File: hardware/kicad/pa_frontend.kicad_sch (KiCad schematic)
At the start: 0 parts

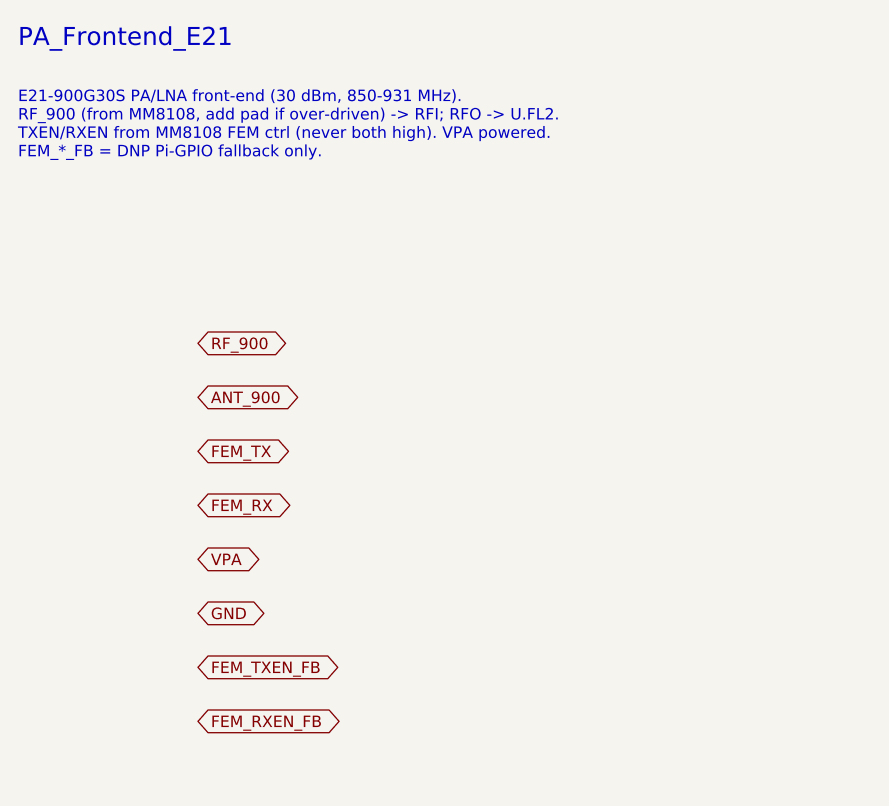
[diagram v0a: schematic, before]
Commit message: Deepen design to component level + fix EEPROM power rail
- Fix: HAT ID EEPROM (U6) now powered from Pi header 3V3 (3V3_PI, pin 1)
  so it is readable at boot before the HAT's own 3V3 comes up (was
  incorrectly on the HAT 3V3 regulator).
- Add docs/SCHEMATIC.md: component-level subcircuits for every block
  (refdes + values + nets) — buck-boost/3V3 FB dividers, MM8108 SPI
  termination/pulls, E21 RF DC-blocks/attenuator pad/T-R pulldowns,
  NEO-M9N active-antenna bias via VCC_RF, ID EEPROM (WP default).
- Add docs/BRINGUP.md: stage-gated power-on + RF test plan (don't key
  the 1W PA until rails/drive-level/FEM-timing verified).
- Add GNSS VCC_RF antenna bias + +3V3_GNSS ferrite to the net list.
- Enrich KiCad sub-sheets with per-block refdes notes and the new nets;
  regenerate scaffold (KiCad 10 format, S-expression balance re-checked).
- BOM: concrete passives (RF DC-blocks, attenuator pad, ferrite, TVS,
  FB dividers, WP jumper).

https://claude.ai/code/session_015nkkW85U3sPf5mcvrsMw7T
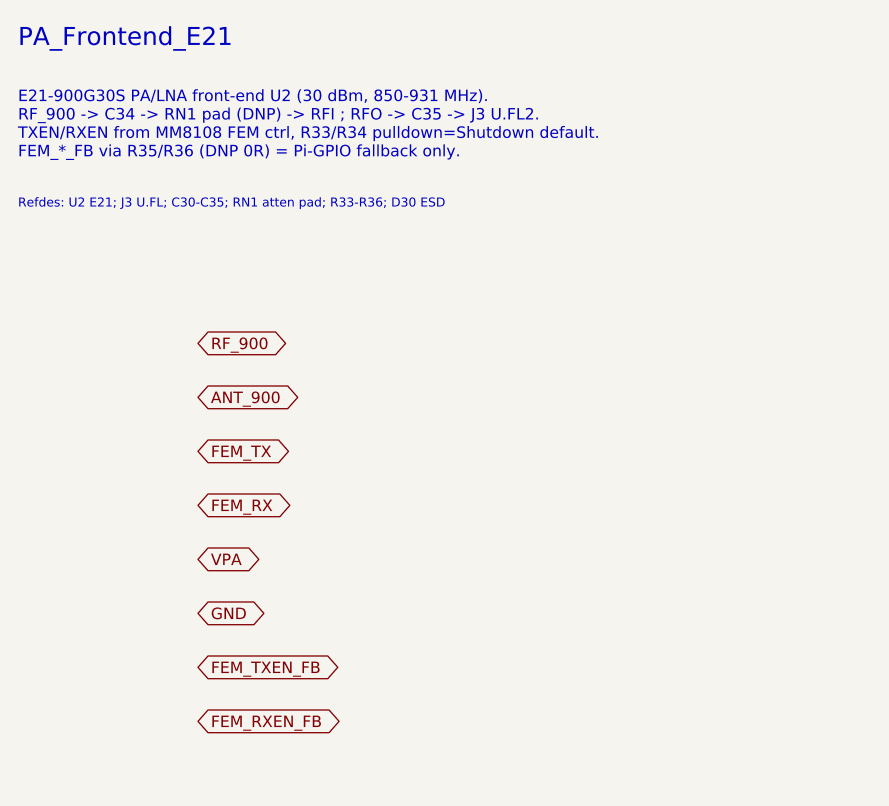
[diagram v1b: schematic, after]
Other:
- note added: "E21-900G30S PA/LNA front-end U2 (30 dBm, 850-931 MHz). RF_900 -> C34 -> RN1 pad (DNP) -> RFI ; RFO -> C35 -> J3 U.FL2. TXEN/RXEN from MM8108 FEM ctrl, R33/R34 pulldown=Shutdown default. FEM_*_FB via R35/R36 (DNP 0R) = Pi-GPIO fallback only."
- note added: "Refdes: U2 E21; J3 U.FL; C30-C35; RN1 atten pad; R33-R36; D30 ESD"
- note removed: "E21-900G30S PA/LNA front-end (30 dBm, 850-931 MHz). RF_900 (from MM8108, add pad if over-driven) -> RFI; RFO -> U.FL2. TXEN/RXEN from MM8108 FEM ctrl (never both high). VPA powered. FEM_*_FB = DNP Pi-GPIO fallback only."
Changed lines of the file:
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@@
 	(paper "A4")
 	(text "PA_Frontend_E21" (exclude_from_sim no) (at 20 15 0) (effects (font (size 2 2) (thickness 0.3)) (justify left top)))
-	(text "E21-900G30S PA/LNA front-end (30 dBm, 850-931 MHz).\nRF_900 (from MM8108, add pad if over-driven) -> RFI; RFO -> U.FL2.\nTXEN/RXEN from MM8108 FEM ctrl (never both high). VPA powered.\nFEM_*_FB = DNP Pi-GPIO fallback only." (exclude_from_sim no) (at 20 22 0) (effects (font (size 1.27 1.27)) (justify left top)))
+	(text "E21-900G30S PA/LNA front-end U2 (30 dBm, 850-931 MHz).\nRF_900 -> C34 -> RN1 pad (DNP) -> RFI ; RFO -> C35 -> J3 U.FL2.\nTXEN/RXEN from MM8108 FEM ctrl, R33/R34 pulldown=Shutdown default.\nFEM_*_FB via R35/R36 (DNP 0R) = Pi-GPIO fallback only." (exclude_from_sim no) (at 20 22 0) (effects (font (size 1.27 1.27)) (justify left top)))
+	(text "Refdes: U2 E21; J3 U.FL; C30-C35; RN1 atten pad; R33-R36; D30 ESD" (exclude_from_sim no) (at 20 34 0) (effects (font (size 1.0 1.0)) (justify left top)))
 	(global_label "RF_900" (shape bidirectional) (at 40 50 0) (fields_autoplaced yes) (effects (font (size 1.27 1.27)) (justify left)))
 	(global_label "ANT_900" (shape bidirectional) (at 40 56 0) (fields_autoplaced yes) (effects (font (size 1.27 1.27)) (justify left)))

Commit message: Add gap-analysis components (datasheet-grounded) + RTC
Read the uploaded datasheets (MM8108-MF15457, E21-900G30S, NEO-M9N-00B)
and resolved the component gaps:

- #1/#2 RESOLVED by the module: MF15457 is self-contained (internal
  clock+PMU+PA); only needs VBAT/VBAT_TX/VDDIO 3.0-3.6 V. No external SoC
  inductors, 1V8/1V2 rails, or TCXO.
- VPA fixed at 5.0 V (E21 needs 4.75-5.25 V, ~620 mA TX, +20 dBm in ->
  +30 dBm out, 12 dB gain). Real pinouts wired (module 38-pin; E21
  pin6=PIN xcvr, pin9=ANT).
- Architecture finding: module has integrated PA + single ANT pin and NO
  hardware T/R FEM line. External E21 now needs (a) ~3-5 dB drive pad,
  (b) T/R control via module GPIO0/1 toggled by OpenMANET FW (or RF-sense
  auto-T/R fallback), and (c) end-product recertification at +30 dBm.

Added components:
- N3 900 MHz harmonic LPF (FL2); N4 inrush soft-start load switch (U10);
  N5 supervisor (U11); N6 radio-rail load switch (U12, OpenMANET
  power-gpios); N7 RF shields; N8 GNSS antenna ESD (D8); N9 status LEDs;
  N10 E21 thermal relief.
- RTC: RV-3028-C7 (U13) on I2C1 0x52 with a soldered rechargeable cell
  (BT1, trickle-charged) per request; added to the device-tree overlay.
- Declined per request: debug UART/JTAG pads, test points.

Updated docs (new COMPONENTS_GAP.md; DECISIONS B1-B9; SCHEMATIC; BOM;
POWER budget), netlist, overlay, and regenerated the KiCad 10 scaffold
with the new nets. Committed the vendor datasheets under hardware/.

https://claude.ai/code/session_015nkkW85U3sPf5mcvrsMw7T
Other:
- note added: "E21-900G30S U2 (VCC=5.0V, ~620mA TX, +20dBm in->+30dBm out). RF_900 (module ANT +22..25dBm) -> C34 -> RN1 ~3-5dB pad -> PIN(6). ANT(9) -> FL2 LPF -> C35 -> J3 U.FL2 (+30dBm harmonic compliance). TX_EN(3)/RX_EN(4) <- PA_TX/RX_CTL; R33/R34 pulldown=Shutdown default."
- note added: "Refdes: U2 E21; J3 U.FL; FL2 LPF; RN1 pad; C30-C35; R33-R36; D30 ESD"
- note removed: "E21-900G30S PA/LNA front-end U2 (30 dBm, 850-931 MHz). RF_900 -> C34 -> RN1 pad (DNP) -> RFI ; RFO -> C35 -> J3 U.FL2. TXEN/RXEN from MM8108 FEM ctrl, R33/R34 pulldown=Shutdown default. FEM_*_FB via R35/R36 (DNP 0R) = Pi-GPIO fallback only."
- note removed: "Refdes: U2 E21; J3 U.FL; C30-C35; RN1 atten pad; R33-R36; D30 ESD"
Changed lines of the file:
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@@
 	(paper "A4")
 	(text "PA_Frontend_E21" (exclude_from_sim no) (at 20 15 0) (effects (font (size 2 2) (thickness 0.3)) (justify left top)))
-	(text "E21-900G30S PA/LNA front-end U2 (30 dBm, 850-931 MHz).\nRF_900 -> C34 -> RN1 pad (DNP) -> RFI ; RFO -> C35 -> J3 U.FL2.\nTXEN/RXEN from MM8108 FEM ctrl, R33/R34 pulldown=Shutdown default.\nFEM_*_FB via R35/R36 (DNP 0R) = Pi-GPIO fallback only." (exclude_from_sim no) (at 20 22 0) (effects (font (size 1.27 1.27)) (justify left top)))
-	(text "Refdes: U2 E21; J3 U.FL; C30-C35; RN1 atten pad; R33-R36; D30 ESD" (exclude_from_sim no) (at 20 34 0) (effects (font (size 1.0 1.0)) (justify left top)))
+	(text "E21-900G30S U2 (VCC=5.0V, ~620mA TX, +20dBm in->+30dBm out).\nRF_900 (module ANT +22..25dBm) -> C34 -> RN1 ~3-5dB pad -> PIN(6).\nANT(9) -> FL2 LPF -> C35 -> J3 U.FL2 (+30dBm harmonic compliance).\nTX_EN(3)/RX_EN(4) <- PA_TX/RX_CTL; R33/R34 pulldown=Shutdown default." (exclude_from_sim no) (at 20 22 0) (effects (font (size 1.27 1.27)) (justify left top)))
+	(text "Refdes: U2 E21; J3 U.FL; FL2 LPF; RN1 pad; C30-C35; R33-R36; D30 ESD" (exclude_from_sim no) (at 20 34 0) (effects (font (size 1.0 1.0)) (justify left top)))
 	(global_label "RF_900" (shape bidirectional) (at 40 50 0) (fields_autoplaced yes) (effects (font (size 1.27 1.27)) (justify left)))
 	(global_label "ANT_900" (shape bidirectional) (at 40 56 0) (fields_autoplaced yes) (effects (font (size 1.27 1.27)) (justify left)))
-	(global_label "FEM_TX" (shape bidirectional) (at 40 62 0) (fields_autoplaced yes) (effects (font (size 1.27 1.27)) (justify left)))
-	(global_label "FEM_RX" (shape bidirectional) (at 40 68 0) (fields_autoplaced yes) (effects (font (size 1.27 1.27)) (justify left)))
+	(global_label "PA_TX_CTL" (shape bidirectional) (at 40 62 0) (fields_autoplaced yes) (effects (font (size 1.27 1.27)) (justify left)))
+	(global_label "PA_RX_CTL" (shape bidirectional) (at 40 68 0) (fields_autoplaced yes) (effects (font (size 1.27 1.27)) (justify left)))
 	(global_label "VPA" (shape bidirectional) (at 40 74 0) (fields_autoplaced yes) (effects (font (size 1.27 1.27)) (justify left)))
 	(global_label "GND" (shape bidirectional) (at 40 80 0) (fields_autoplaced yes) (effects (font (size 1.27 1.27)) (justify left)))

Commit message: Make E21 PA a DNP/optional Variant B; default to module-only
Deployment is ground/handheld/vehicle (NLOS), where the E21's +3 dB buys
only ~20% range (LINK_BUDGET) against ~620 mA + heat + recert + RX-rate
risk. So restructure as one PCB with two BOM builds:

- Variant A (DEFAULT): module-only ~27 dBm via OpenMANET BCF. E21,
  buck-boost (VPA), LPF and drive pad are DNP; an RF bypass (C_BYP)
  carries the module ANT straight to U.FL #2. Low power (~0.35 A), good
  for battery handhelds, stays on the module's modular cert.
- Variant B (OPTIONAL): populate E21 + VPA + LPF + T/R for +30 dBm
  extended range (fixed/elevated LoS); remove C_BYP; needs custom-BCF
  FEM GPIO control + end-product recert. No respin required.

Updated DECISIONS (B5/B10 resolved + new §C variants & order), SCHEMATIC,
POWER (default-build budget), BOM (variant tags + C_BYP), netlist, README,
and regenerated the KiCad scaffold (bypass net + silk tags).

https://claude.ai/code/session_015nkkW85U3sPf5mcvrsMw7T
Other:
- note added: "E21-900G30S U2 -- VARIANT B (DNP DEFAULT). +30dBm extended-range opt. Variant A (default): module ANT -> C_BYP RF bypass -> J3 U.FL2 (no PA). Variant B: RF_900 -> C34 -> RN1 ~3-5dB pad -> PIN(6); ANT(9)->FL2->U.FL2. TX_EN(3)/RX_EN(4) <- PA_TX/RX_CTL (BCF); R33/R34 pulldown=off default."
- note added: "Refdes: U2 E21; C_BYP bypass(VarA); J3 U.FL; FL2 LPF; RN1 pad; C30-C35; R33-R36; D30 ESD"
- note removed: "E21-900G30S U2 (VCC=5.0V, ~620mA TX, +20dBm in->+30dBm out). RF_900 (module ANT +22..25dBm) -> C34 -> RN1 ~3-5dB pad -> PIN(6). ANT(9) -> FL2 LPF -> C35 -> J3 U.FL2 (+30dBm harmonic compliance). TX_EN(3)/RX_EN(4) <- PA_TX/RX_CTL; R33/R34 pulldown=Shutdown default."
- note removed: "Refdes: U2 E21; J3 U.FL; FL2 LPF; RN1 pad; C30-C35; R33-R36; D30 ESD"
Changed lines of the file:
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@@
 	(paper "A4")
 	(text "PA_Frontend_E21" (exclude_from_sim no) (at 20 15 0) (effects (font (size 2 2) (thickness 0.3)) (justify left top)))
-	(text "E21-900G30S U2 (VCC=5.0V, ~620mA TX, +20dBm in->+30dBm out).\nRF_900 (module ANT +22..25dBm) -> C34 -> RN1 ~3-5dB pad -> PIN(6).\nANT(9) -> FL2 LPF -> C35 -> J3 U.FL2 (+30dBm harmonic compliance).\nTX_EN(3)/RX_EN(4) <- PA_TX/RX_CTL; R33/R34 pulldown=Shutdown default." (exclude_from_sim no) (at 20 22 0) (effects (font (size 1.27 1.27)) (justify left top)))
-	(text "Refdes: U2 E21; J3 U.FL; FL2 LPF; RN1 pad; C30-C35; R33-R36; D30 ESD" (exclude_from_sim no) (at 20 34 0) (effects (font (size 1.0 1.0)) (justify left top)))
+	(text "E21-900G30S U2 -- VARIANT B (DNP DEFAULT). +30dBm extended-range opt.\nVariant A (default): module ANT -> C_BYP RF bypass -> J3 U.FL2 (no PA).\nVariant B: RF_900 -> C34 -> RN1 ~3-5dB pad -> PIN(6); ANT(9)->FL2->U.FL2.\nTX_EN(3)/RX_EN(4) <- PA_TX/RX_CTL (BCF); R33/R34 pulldown=off default." (exclude_from_sim no) (at 20 22 0) (effects (font (size 1.27 1.27)) (justify left top)))
+	(text "Refdes: U2 E21; C_BYP bypass(VarA); J3 U.FL; FL2 LPF; RN1 pad; C30-C35; R33-R36; D30 ESD" (exclude_from_sim no) (at 20 34 0) (effects (font (size 1.0 1.0)) (justify left top)))
 	(global_label "RF_900" (shape bidirectional) (at 40 50 0) (fields_autoplaced yes) (effects (font (size 1.27 1.27)) (justify left)))
 	(global_label "ANT_900" (shape bidirectional) (at 40 56 0) (fields_autoplaced yes) (effects (font (size 1.27 1.27)) (justify left)))
-	(global_label "PA_TX_CTL" (shape bidirectional) (at 40 62 0) (fields_autoplaced yes) (effects (font (size 1.27 1.27)) (justify left)))
-	(global_label "PA_RX_CTL" (shape bidirectional) (at 40 68 0) (fields_autoplaced yes) (effects (font (size 1.27 1.27)) (justify left)))
-	(global_label "VPA" (shape bidirectional) (at 40 74 0) (fields_autoplaced yes) (effects (font (size 1.27 1.27)) (justify left)))
-	(global_label "GND" (shape bidirectional) (at 40 80 0) (fields_autoplaced yes) (effects (font (size 1.27 1.27)) (justify left)))
-	(global_label "FEM_TXEN_FB" (shape bidirectional) (at 40 86 0) (fields_autoplaced yes) (effects (font (size 1.27 1.27)) (justify left)))
-	(global_label "FEM_RXEN_FB" (shape bidirectional) (at 40 92 0) (fields_autoplaced yes) (effects (font (size 1.27 1.27)) (justify left)))
+	(global_label "C_BYP" (shape bidirectional) (at 40 62 0) (fields_autoplaced yes) (effects (font (size 1.27 1.27)) (justify left)))
+	(global_label "PA_TX_CTL" (shape bidirectional) (at 40 68 0) (fields_autoplaced yes) (effects (font (size 1.27 1.27)) (justify left)))
+	(global_label "PA_RX_CTL" (shape bidirectional) (at 40 74 0) (fields_autoplaced yes) (effects (font (size 1.27 1.27)) (justify left)))
+	(global_label "VPA" (shape bidirectional) (at 40 80 0) (fields_autoplaced yes) (effects (font (size 1.27 1.27)) (justify left)))
+	(global_label "GND" (shape bidirectional) (at 40 86 0) (fields_autoplaced yes) (effects (font (size 1.27 1.27)) (justify left)))
+	(global_label "FEM_TXEN_FB" (shape bidirectional) (at 40 92 0) (fields_autoplaced yes) (effects (font (size 1.27 1.27)) (justify left)))
+	(global_label "FEM_RXEN_FB" (shape bidirectional) (at 40 98 0) (fields_autoplaced yes) (effects (font (size 1.27 1.27)) (justify left)))
 )

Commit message: Pivot to MM8108-M20 primary / MF15457 fallback; retire external E21
Per the decision to make the MM8108-M20 the primary radio (with MF15457
as the build-today fallback) and retire the external E21 PA path:

Design:
- One radio site fed by the shared SPI/control nets accepts either module.
- Removed the E21 PA, 5V buck-boost (VPA), harmonic LPF, drive pad, T/R
  control, RF-sense VOX, and RF bypass. Both modules drive the antenna
  directly (M20 = integrated 28.5 dBm PA + 902-928 SAW, certified;
  MF15457 = ~27 dBm). Power collapses to a single 3V3 rail.
- Header GPIO4/6 (old FEM fallback) revert to spares; GPIO12/13 drive the
  status LEDs.
- M20 pinout/power/footprint held at placeholder pending its datasheet
  (B12); MF15457 pin-level detail stays the concrete baseline.

Docs updated: DECISIONS (A3 superseded, B11/B12 added, B2-B5/B10 retired,
new radio-options table + order), DESIGN, SCHEMATIC, POWER, RF, BOM,
INTERFACES, COMPONENTS_GAP, LINK_BUDGET, FIRMWARE_PA, BRINGUP, MECHANICAL,
README. Netlist, KiCad scaffold (sheets/silk/root note), and the OpenMANET
overlay/README updated to match. Scaffold regenerated and validated.

https://claude.ai/code/session_015nkkW85U3sPf5mcvrsMw7T
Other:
- note added: "900MHz RF OUTPUT / ANTENNA (E21 PA retired, B11). Radio ANT -> RF_900 -> C35 100pF DC-block -> ANT_900 -> J3 U.FL2. FL2 optional LPF = DNP (M20 has integ. SAW; MF15457 modular-certified). D30 low-C RF ESD clamp at the connector. Short 50ohm microstrip."
- note added: "RF_Out_Antenna"
- note added: "Refdes: J3 U.FL; C35 DC-block; FL2 LPF(DNP); D30 ESD"
- note removed: "E21-900G30S U2 -- VARIANT B (DNP DEFAULT). +30dBm extended-range opt. Variant A (default): module ANT -> C_BYP RF bypass -> J3 U.FL2 (no PA). Variant B: RF_900 -> C34 -> RN1 ~3-5dB pad -> PIN(6); ANT(9)->FL2->U.FL2. TX_EN(3)/RX_EN(4) <- PA_TX/RX_CTL (BCF); R33/R34 pulldown=off default."
- note removed: "PA_Frontend_E21"
- note removed: "Refdes: U2 E21; C_BYP bypass(VarA); J3 U.FL; FL2 LPF; RN1 pad; C30-C35; R33-R36; D30 ESD"
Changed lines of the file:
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@@
 	(generator_version "10.0")
 	(paper "A4")
-	(text "PA_Frontend_E21" (exclude_from_sim no) (at 20 15 0) (effects (font (size 2 2) (thickness 0.3)) (justify left top)))
-	(text "E21-900G30S U2 -- VARIANT B (DNP DEFAULT). +30dBm extended-range opt.\nVariant A (default): module ANT -> C_BYP RF bypass -> J3 U.FL2 (no PA).\nVariant B: RF_900 -> C34 -> RN1 ~3-5dB pad -> PIN(6); ANT(9)->FL2->U.FL2.\nTX_EN(3)/RX_EN(4) <- PA_TX/RX_CTL (BCF); R33/R34 pulldown=off default." (exclude_from_sim no) (at 20 22 0) (effects (font (size 1.27 1.27)) (justify left top)))
-	(text "Refdes: U2 E21; C_BYP bypass(VarA); J3 U.FL; FL2 LPF; RN1 pad; C30-C35; R33-R36; D30 ESD" (exclude_from_sim no) (at 20 34 0) (effects (font (size 1.0 1.0)) (justify left top)))
+	(text "RF_Out_Antenna" (exclude_from_sim no) (at 20 15 0) (effects (font (size 2 2) (thickness 0.3)) (justify left top)))
+	(text "900MHz RF OUTPUT / ANTENNA (E21 PA retired, B11).\nRadio ANT -> RF_900 -> C35 100pF DC-block -> ANT_900 -> J3 U.FL2.\nFL2 optional LPF = DNP (M20 has integ. SAW; MF15457 modular-certified).\nD30 low-C RF ESD clamp at the connector. Short 50ohm microstrip." (exclude_from_sim no) (at 20 22 0) (effects (font (size 1.27 1.27)) (justify left top)))
+	(text "Refdes: J3 U.FL; C35 DC-block; FL2 LPF(DNP); D30 ESD" (exclude_from_sim no) (at 20 34 0) (effects (font (size 1.0 1.0)) (justify left top)))
 	(global_label "RF_900" (shape bidirectional) (at 40 50 0) (fields_autoplaced yes) (effects (font (size 1.27 1.27)) (justify left)))
 	(global_label "ANT_900" (shape bidirectional) (at 40 56 0) (fields_autoplaced yes) (effects (font (size 1.27 1.27)) (justify left)))
-	(global_label "C_BYP" (shape bidirectional) (at 40 62 0) (fields_autoplaced yes) (effects (font (size 1.27 1.27)) (justify left)))
-	(global_label "PA_TX_CTL" (shape bidirectional) (at 40 68 0) (fields_autoplaced yes) (effects (font (size 1.27 1.27)) (justify left)))
-	(global_label "PA_RX_CTL" (shape bidirectional) (at 40 74 0) (fields_autoplaced yes) (effects (font (size 1.27 1.27)) (justify left)))
-	(global_label "VPA" (shape bidirectional) (at 40 80 0) (fields_autoplaced yes) (effects (font (size 1.27 1.27)) (justify left)))
-	(global_label "GND" (shape bidirectional) (at 40 86 0) (fields_autoplaced yes) (effects (font (size 1.27 1.27)) (justify left)))
-	(global_label "FEM_TXEN_FB" (shape bidirectional) (at 40 92 0) (fields_autoplaced yes) (effects (font (size 1.27 1.27)) (justify left)))
-	(global_label "FEM_RXEN_FB" (shape bidirectional) (at 40 98 0) (fields_autoplaced yes) (effects (font (size 1.27 1.27)) (justify left)))
+	(global_label "GND" (shape bidirectional) (at 40 62 0) (fields_autoplaced yes) (effects (font (size 1.27 1.27)) (justify left)))
 )
